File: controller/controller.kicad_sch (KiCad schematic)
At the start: 58 parts, among them J11 Conn_ARM_JTAG_SWD_10, J12 GRPB072VWQS-RC, J6 USB_C_Receptacle_USB2.0_16P, J7 USB_C_Receptacle_USB2.0_16P, J8 GRPB072VWQS-RC, J9 GRPB072VWQS-RC, U1 STM32G474RCTx, U10 PI5C3257, U11 QSBT40-7-F, U12 QSBT40-7-F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

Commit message: Controller and firwmare most pins in sync
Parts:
- added D13, D14, D15, D16, D17, D18, D19, D21: LED, symbol Device:LED
- added D20, D22: LED_ARGB, symbol Device:LED_ARGB
- added R25, R26: 0R, Resistor_SMD:R_0402_1005Metric, symbol Device:R_Small
- added RV2, RV3: R_Potentiometer, symbol Device:R_Potentiometer
- R69: footprint (none) -> Resistor_SMD:R_0402_1005Metric
- R70, R73: footprint Resistor_SMD:R_0603_1608Metric -> Resistor_SMD:R_0402_1005Metric
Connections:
- net +3V3: now also D16.2 (A), D17.2 (A), D18.2 (A), D19.2 (A), D21.2 (A), D22.1 (A), R26.2, RV2.1, RV3.1
- net +5V: now also R25.2
- net ADC2_IN10: no longer U1.6 (PF1)
- net ADC2_IN11: now also D19.1 (K)
- net Earth: now also RV2.3, RV3.3
- net FB_B: now also U1.6 (PF1)
- net FB_D: now also U1.22 (PC4)
- net HI_4: now also U8.13 (I1c); no longer U8.3 (I1a)
- net HI_5: now also U8.3 (I1a); no longer U8.13 (I1c)
- net HRTIM1_EEV3: no longer U1.60 (PB7)
- net HRTIM1_EEV5: no longer U1.62 (PB9)
- net HRTIM1_EEV6: no longer U1.58 (PB5)
- net HRTIM1_FLT3: no longer U1.30 (PB10)
- net LI_4: now also U8.10 (I1d); no longer U8.6 (I1b)
- net LI_5: now also U8.6 (I1b); no longer U8.10 (I1d)
- net PC2: now also D21.1 (K)
- net pwm_led5 pot2: now reaches U1.17 (PA3)
- net pwm_led5 pot2: now also D17.1 (K), D22.3 (GK), RV2.2
- net pwm_led6 pot3: now reaches U1.25 (PB1)
- net pwm_led6 pot3: now also D18.1 (K), D22.4 (BK), RV3.2
- new net: D13.2 (A), D14.2 (A), D15.2 (A), D20.1 (A), R25.1, R26.1
- new net pwm_led1: D13.1 (K), D20.2 (RK), U1.58 (PB5)
- new net pwm_led2: D14.1 (K), D20.3 (GK), U1.60 (PB7)
- new net pwm_led3: D15.1 (K), D20.4 (BK), U1.62 (PB9)
- new net pwm_led4: D16.1 (K), D22.2 (RK), U1.30 (PB10)
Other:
- note removed: "Update to match firmware"
- moved on the sheet: R72, U8

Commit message: Controller - some more changes
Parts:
- added C29, C30, C31, C32, C34: 10nF, Capacitor_SMD:C_0402_1005Metric, symbol Device:C_Small
- added R28, R29, R30, R32: 0R, Resistor_SMD:R_0402_1005Metric, symbol Device:R_Small
- added R33, R34, R36, R37, R38, R40, R47, R48: ?, Resistor_SMD:R_0402_1005Metric, symbol Device:R_Small
- D20: value LED_ARGB -> CLMUD-FKC-CHJNPM569ABB845343; footprint (none) -> Library:LED_Cree-PLCC4_1.5x1.5mm
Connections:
- net Current_sense_1B: now also R28.2
- net Current_sense_2B: now also R29.2
- net Current_sense_4: now also R29.1
- net Current_sense_5: now also R28.1
- net Earth: now also C29.2, C30.2, C31.2, C32.2, C34.2
- net FB_A: now also R30.2, R32.2
- net PB2: now also C34.1
- net PC2: now also C32.1, R48.1; no longer D21.1 (K)
- net pwm_led1: now also R33.1; no longer D13.1 (K), D20.2 (RK)
- net pwm_led2: now also R34.1; no longer D14.1 (K), D20.3 (GK)
- net pwm_led3: now also R36.1; no longer D15.1 (K), D20.4 (BK)
- net pwm_led4: now also R37.1; no longer D16.1 (K), D22.2 (RK)
- net pwm_led5 pot2: now also C30.1, R30.1, R38.1; no longer D17.1 (K), D22.3 (GK)
- net pwm_led6 pot3: now also C31.1, R40.1; no longer D18.1 (K), D22.4 (BK)
- net ADC2_IN11: no longer names the net of D19.1 (K)
- net ADC2_IN11: now also R47.2; no longer U1.23 (PC5)
- new net: D13.1 (K), D20.2 (RK), R33.2
- new net: D16.1 (K), D22.2 (RK), R37.2
- new net: D18.1 (K), D22.4 (BK), R40.2
- new net: D17.1 (K), D22.3 (GK), R38.2
- new net: D15.1 (K), D20.4 (BK), R36.2
- new net: D14.1 (K), D20.3 (GK), R34.2
- new net: D21.1 (K), R48.2
- new net pwm_led7: C29.1, R32.1, R47.1, U1.23 (PC5)
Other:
- note added: "Kolla så esp kan output på LED-pinnar"
- note added: "Route FB_A"
- moved on the sheet: RV2

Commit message: Controller - more changes
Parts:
- D22: footprint (none) -> Library:LED_Cree-PLCC4_1.5x1.5mm
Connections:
- net PC2: now also R37.1; no longer R48.1
- net pwm_led4: now also R38.1; no longer R37.1
- net pwm_led5 pot2: now also R48.1; no longer R38.1
- net pwm_led6 pot3: now also R47.1; no longer R40.1
- net pwm_led7: now also R40.1; no longer R47.1
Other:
- sheet esp32c6 ports: added B_BOOT, G, R; removed none
- note removed: "V_{GS} >= 100V"
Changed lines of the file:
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@@
 	(wire
 		(pts
-			(xy 171.45 170.18) (xy 186.69 170.18)
-		)
-		(stroke
-			(width 0)
-			(type default)
-		)
-	)
-	(wire
-		(pts
 			(xy 427.99 72.39) (xy 454.66 72.39)
 		)
@@
 	(wire
 		(pts
+			(xy 177.8 172.72) (xy 171.45 172.72)
+		)
+		(stroke
+			(width 0)
+			(type default)
+		)
+	)
+	(wire
+		(pts
 			(xy 167.64 97.79) (xy 179.07 97.79)
 		)
@@
 	(wire
 		(pts
-			(xy 55.88 407.67) (xy 63.5 407.67)
-		)
-		(stroke
-			(width 0)
-			(type default)
-		)
-	)
-	(wire
-		(pts
 			(xy 434.34 163.83) (xy 438.15 163.83)
 		)
@@
 	(wire
 		(pts
+			(xy 182.88 170.18) (xy 171.45 170.18)
+		)
+		(stroke
+			(width 0)
+			(type default)
+		)
+	)
+	(wire
+		(pts
 			(xy 167.64 77.47) (xy 185.42 77.47)
 		)
@@
 	(wire
 		(pts
-			(xy 171.45 167.64) (xy 193.04 167.64)
+			(xy 171.45 163.83) (xy 193.04 163.83)
 		)
 		(stroke
@@
 	(wire
 		(pts
+			(xy 171.45 166.37) (xy 186.69 166.37)
+		)
+		(stroke
+			(width 0)
+			(type default)
+		)
+	)
+	(wire
+		(pts
 			(xy 303.53 281.94) (xy 303.53 280.67)
 		)
@@
 	(wire
 		(pts
+			(xy 182.88 175.26) (xy 171.45 175.26)
+		)
+		(stroke
+			(width 0)
+			(type default)
+		)
+	)
+	(wire
+		(pts
 			(xy 88.9 278.13) (xy 76.2 278.13)
 		)
@@
 	(text "Kolla så esp kan output på LED-pinnar"
 		(exclude_from_sim no)
-		(at 136.398 168.91 0)
+		(at 141.478 188.976 0)
 		(effects
 			(font
@@
 		)
 	)
-	(text "V_{GS} >= 100V"
-		(exclude_from_sim no)
-		(at 72.644 406.4 0)
-		(effects
-			(font
-				(size 1.27 1.27)
-			)
-		)
-	)
 	(text "page 37 layout i https://www.ti.com/lit/ds/symlink/lm5168.pdf?ts=1714923464346"
 		(exclude_from_sim no)
@@
 	)
 	(label "pwm_led5 pot2"
-		(at 430.53 185.42 270)
+		(at 450.85 185.42 270)
 		(fields_autoplaced yes)
 		(effects
@@
 		)
 	)
+	(label "pwm_led4"
+		(at 182.88 175.26 180)
+		(fields_autoplaced yes)
+		(effects
+			(font
+				(size 1.27 1.27)
+			)
+			(justify right bottom)
+		)
+	)
 	(label "NTC_2"
 		(at 124.46 80.01 0)
@@
 	)
 	(label "pwm_led4"
-		(at 424.18 185.42 270)
+		(at 430.53 185.42 270)
 		(fields_autoplaced yes)
 		(effects
@@
 	)
 	(label "pwm_led7"
-		(at 444.5 185.42 270)
+		(at 438.15 185.42 270)
 		(fields_autoplaced yes)
 		(effects
@@
 	)
 	(label "PC2"
-		(at 450.85 185.42 270)
+		(at 424.18 185.42 270)
 		(fields_autoplaced yes)
 		(effects
@@
 	)
 	(label "STM32_NRST_TO_ESP"
-		(at 193.04 167.64 180)
+		(at 193.04 163.83 180)
+		(fields_autoplaced yes)
+		(effects
+			(font
+				(size 1.27 1.27)
+			)
+			(justify right bottom)
+		)
+	)
+	(label "pwm_led7"
+		(at 182.88 170.18 180)
 		(fields_autoplaced yes)
 		(effects
@@
 	)
 	(label "STM32_BOOT0"
-		(at 186.69 170.18 180)
+		(at 186.69 166.37 180)
 		(fields_autoplaced yes)
 		(effects
@@
 		)
 	)
+	(label "PC2"
+		(at 177.8 172.72 180)
+		(fields_autoplaced yes)
+		(effects
+			(font
+				(size 1.27 1.27)
+			)
+			(justify right bottom)
+		)
+	)
 	(label "STM32_SWC"
 		(at 181.61 85.09 180)
@@
 	)
 	(label "pwm_led6 pot3"
-		(at 438.15 185.42 270)
+		(at 444.5 185.42 270)
 		(fields_autoplaced yes)
 		(effects
@@
 			)
 		)
-		(property "Footprint" ""
+		(property "Footprint" "Library:LED_Cree-PLCC4_1.5x1.5mm"
 			(at 412.75 166.37 0)
 			(effects
@@
 	)
 	(symbol
-		(lib_id "power:Earth")
-		(at 55.88 407.67 0)
-		(unit 1)
-		(exclude_from_sim no)
-		(in_bom yes)
-		(on_board yes)
-		(dnp no)
-		(fields_autoplaced yes)
-		(property "Reference" "#PWR0122"
-			(at 55.88 414.02 0)
-			(effects
-				(font
-					(size 1.27 1.27)
-				)
-				(hide yes)
-			)
-		)
-		(property "Value" "Earth"
-			(at 55.88 411.48 0)
-			(effects
-				(font
-					(size 1.27 1.27)
-				)
-				(hide yes)
-			)
-		)
-		(property "Footprint" ""
-			(at 55.88 407.67 0)
-			(effects
-				(font
-					(size 1.27 1.27)
-				)
-				(hide yes)
-			)
-		)
-		(property "Datasheet" "~"
-			(at 55.88 407.67 0)
-			(effects
-				(font
-					(size 1.27 1.27)
-				)
-				(hide yes)
-			)
-		)
-		(property "Description" ""
-			(at 55.88 407.67 0)
-			(effects
-				(font
-					(size 1.27 1.27)
-				)
-				(hide yes)
-			)
-		)
-		(pin "1"
-		)
-		(instances
-			(project "controller"
-				(path "/5b092a03-7e3e-4df1-ad91-2ac0e362f857"
-					(reference "#PWR0122")
-					(unit 1)
-				)
-			)
-		)
-	)
-	(symbol
 		(lib_id "74xx:74LS257")
 		(at 251.46 172.72 0)
@@
 		(at 128.27 162.56)
 		(size 43.18 13.97)
+		(fields_autoplaced yes)
 		(stroke
 			(width 0.1524)
@@
 		)
 		(property "Sheetname" "esp32c6"
-			(at 145.034 168.656 0)
+			(at 128.27 161.8484 0)
 			(effects
 				(font
@@
 		)
 		(property "Sheetfile" "esp32c6.kicad_sch"
-			(at 136.906 173.482 0)
+			(at 128.27 177.1146 0)
 			(effects
 				(font
@@
 		)
 		(pin "GPIO21" bidirectional
-			(at 171.45 170.18 0)
+			(at 171.45 166.37 0)
 			(effects
 				(font
@@
 		)
 		(pin "GPIO20" bidirectional
-			(at 171.45 167.64 0)
+			(at 171.45 163.83 0)
 			(effects
 				(font
@@
 			)
 		)
+		(pin "B_BOOT" bidirectional
+			(at 171.45 175.26 0)
+			(effects
+				(font
+					(size 1.27 1.27)
+				)
+				(justify right)
+			)
+		)
+		(pin "G" input
+			(at 171.45 172.72 0)
+			(effects
+				(font
+					(size 1.27 1.27)
+				)
+				(justify right)
+			)
+		)
+		(pin "R" output
+			(at 171.45 170.18 0)
+			(effects
+				(font
+					(size 1.27 1.27)
+				)
+				(justify right)
+			)
+		)

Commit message: Controller - Route mcu pins
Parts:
- removed R97: 100k, Resistor_SMD:R_0402_1005Metric, symbol Device:R_Small
- added C36: 10nF, Capacitor_SMD:C_0402_1005Metric, symbol Device:C_Small
- added R67: 1k, Resistor_SMD:R_0402_1005Metric, symbol Device:R_Small
- added SW3: Boot, symbol Switch:SW_Push
- added SW4: Reset, symbol Switch:SW_Push
- added U14: QSBT40-7-F, Package_TO_SOT_SMD:SOT-363_SC-70-6, symbol Library:QSBT40-7-F
- J11: footprint (none) -> Connector_PinHeader_1.27mm:PinHeader_2x05_P1.27mm_Vertical_SMD
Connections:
- net +3V3: now also SW3.1, U14.5 (VCC)
- net CC1_MCU: now also U12.3 (DL3), U12.4 (DL2); no longer U13.6 (DL1)
- net CC2_MCU: now also U12.1 (DL4), U12.6 (DL1); no longer U13.4 (DL2)
- net Earth: now also C36.2, SW4.2, U14.2 (GND)
- net FB_A: now also U14.4 (DL2), U14.6 (DL1); no longer U12.6 (DL1)
- net FB_B: now also U14.1 (DL4), U14.3 (DL3); no longer U12.4 (DL2)
- net FB_C: now also U13.1 (DL4); no longer U12.3 (DL3)
- net FB_D: now also U13.6 (DL1); no longer U12.1 (DL4)
- net PA4: now also U13.4 (DL2); no longer U13.3 (DL3)
- net PA5: now also U13.3 (DL3); no longer U13.1 (DL4)
- net STM32_BOOT0: now also R67.2; no longer U1.61 (PB8)
- net STM32_NRST_TO_CON: no longer R96.1, U9.4 (Pin_4)
- net STM32_NRST: now reaches C19.1, R69.2, R70.2, R73.2, U1.7 (PG10)
- net STM32_NRST: now also R96.1, U9.4 (Pin_4), SW4.1
- new net: C36.1, R67.1, SW3.2, U1.61 (PB8)
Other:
- note removed: "Kolla så esp kan output på LED-pinnar"
- moved on the sheet: R69, R70, R73, R94, R95, R96, U12A, U12B, U12C, U12D, U12E, U13A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

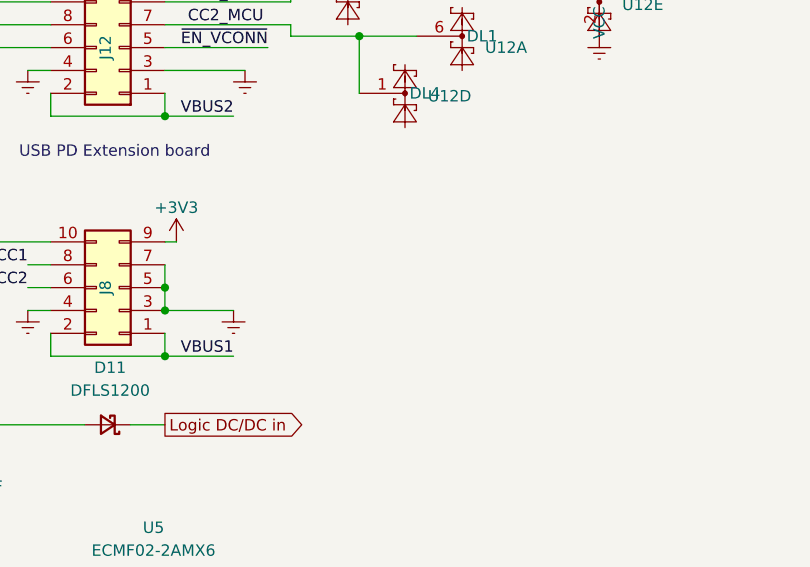
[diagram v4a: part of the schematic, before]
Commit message: Controller - Even more pins
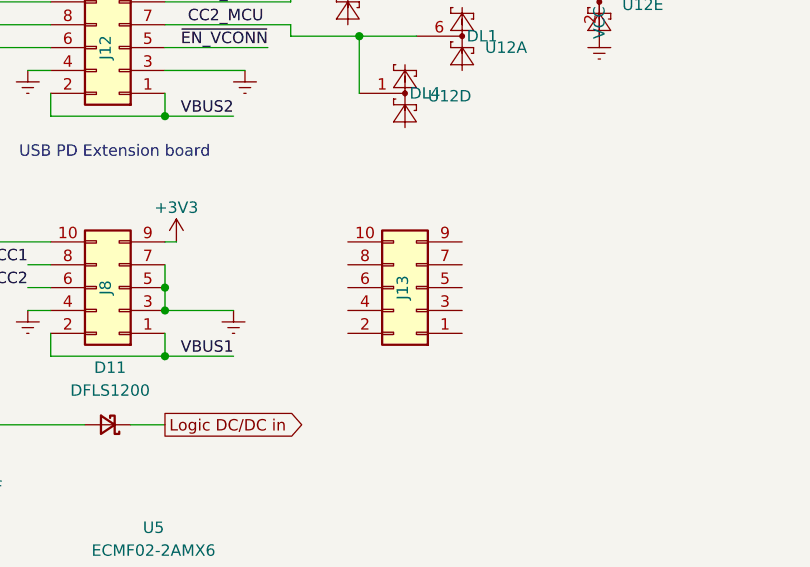
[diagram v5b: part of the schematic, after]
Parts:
- added J13: GRPB072VWQS-RC, Connector_PinHeader_1.27mm:PinHeader_2x05_P1.27mm_Vertical_SMD, symbol Connector_Generic:Conn_02x05_Odd_Even
- R74, R75: footprint Resistor_SMD:R_0805_1005Metric -> Resistor_SMD:R_0805_2012Metric
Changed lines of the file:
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@@
 			)
 		)
-		(property "Footprint" "Resistor_SMD:R_0805_1005Metric"
+		(property "Footprint" "Resistor_SMD:R_0805_2012Metric"
 			(at 332.74 30.48 0)
 			(effects
@@
 			)
 		)
-		(property "Footprint" "Resistor_SMD:R_0805_1005Metric"
+		(property "Footprint" "Resistor_SMD:R_0805_2012Metric"
 			(at 332.74 26.67 0)
 			(effects
@@
 					(unit 1)
 				)
+			)
+		)
+	)
+	(symbol
+		(lib_id "Connector_Generic:Conn_02x05_Odd_Even")
+		(at 104.14 320.04 180)
+		(unit 1)
+		(exclude_from_sim no)
+		(in_bom yes)
+		(on_board yes)
+		(dnp no)
+		(property "Reference" "J13"
+			(at 102.616 320.04 90)
+			(effects
+				(font
+					(size 1.27 1.27)
+				)
+			)
+		)
+		(property "Value" "GRPB072VWQS-RC"
+			(at 102.616 319.786 90)
+			(effects
+				(font
+					(size 1.27 1.27)
+				)
+				(hide yes)
+			)
+		)
+		(property "Footprint" "Connector_PinHeader_1.27mm:PinHeader_2x05_P1.27mm_Vertical_SMD"
+			(at 104.14 320.04 0)
+			(effects
+				(font
+					(size 1.27 1.27)
+				)
+				(hide yes)
+			)
+		)
+		(property "Datasheet" "~"
+			(at 104.14 320.04 0)
+			(effects
+				(font
+					(size 1.27 1.27)
+				)
+				(hide yes)
+			)
+		)
+		(property "Description" "Generic connector, double row, 02x05, odd/even pin numbering scheme (row 1 odd numbers, row 2 even numbers), script generated (kicad-library-utils/schlib/autogen/connector/)"
+			(at 104.14 320.04 0)
+			(effects
+				(font
+					(size 1.27 1.27)
+				)
+				(hide yes)
+			)
+		)
+		(pin "3"
+		)
+		(pin "2"
+		)
+		(pin "1"
+		)
+		(pin "6"
+		)
+		(pin "4"
+		)
+		(pin "5"
+		)
+		(pin "8"
+		)
+		(pin "9"
+		)
+		(pin "7"
+		)
+		(pin "10"
+		)
+		(instances
+			(project "controller"
+				(path "/5b092a03-7e3e-4df1-ad91-2ac0e362f857"
+					(reference "J13")
+					(unit 1)
+				)

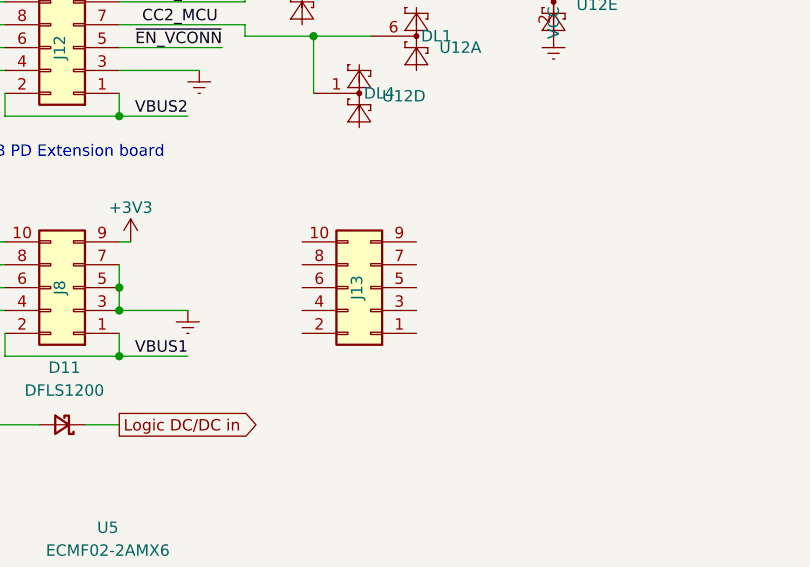
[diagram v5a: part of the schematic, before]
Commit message: Controller - Start work on vbus connection, improve rgb-led placement
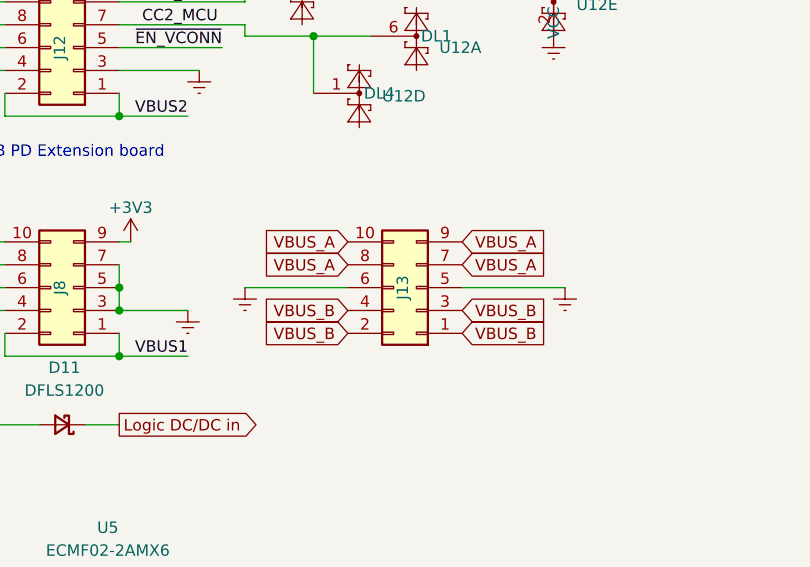
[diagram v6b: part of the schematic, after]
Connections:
- net Earth: now also J13.5 (Pin_5), J13.6 (Pin_6)
- net VBUS_B: now reaches J13.1 (Pin_1)
- net VBUS_B: now also J13.2 (Pin_2), J13.3 (Pin_3), J13.4 (Pin_4)
- net VBUS_A: now reaches J13.10 (Pin_10)
- net VBUS_A: now also J13.7 (Pin_7), J13.8 (Pin_8), J13.9 (Pin_9)
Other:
- moved on the sheet: J13

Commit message: Controller - Setup clearance, place rgb led resistors, some more routing and step down current sense
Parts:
- added R118, R119, R120, R121, R122, R123: 1k, Resistor_SMD:R_0402_1005Metric, symbol Device:R_Small
- added R124, R125, R126, R127, R128, R129: 10k, Resistor_SMD:R_0402_1005Metric, symbol Device:R_Small
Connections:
- net Current_sense_1B is gone; now on net Current_sense_1A: R28.2, U1.9 (PC1)
- net Current_sense_1A: now also U14.3 (DL3), U14.4 (DL2), R122.2, R123.2, R128.2, R129.2
- net Current_sense_2: now also R118.2, R124.2; no longer U10.4 (Za)
- net Current_sense_3: now also R119.2, R125.2; no longer U10.7 (Zb)
- net Current_sense_4: now also R120.2, R126.2; no longer U10.12 (Zc)
- net Current_sense_5: now also R121.2, R127.2; no longer U10.9 (Zd)
- net Earth: now also R124.1, R125.1, R126.1, R127.1, R128.1, R129.1
- net FB_A: no longer U14.4 (DL2)
- net FB_B: no longer U14.3 (DL3)
- new net: R119.1, U10.7 (Zb)
- new net: R121.1, U10.9 (Zd)
- new net: R118.1, U10.4 (Za)
- new net: R120.1, U10.12 (Zc)
- new net hb-card1/Current_sense_xA: R122.1
- new net hb-card1/Current_sense_xB: R123.1
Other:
- note added: "DIODES for CS1!!!! | v"
- moved on the sheet: D12, R74, R75, U13C, U14B, U14C

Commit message: Controller - Change current sensor
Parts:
- removed R119, R120, R121, R122, R123: 1k, Resistor_SMD:R_0402_1005Metric, symbol Device:R_Small
- removed R124, R125, R126, R127, R128, R129: 10k, Resistor_SMD:R_0402_1005Metric, symbol Device:R_Small
- removed U10: PI5C3257, Package_DFN_QFN:TQFN-16-1EP_3x3mm_P0.5mm_EP1.6x1.6mm, symbol 74xx:74LS257
- added C40: 10nF, Capacitor_SMD:C_0402_1005Metric, symbol Device:C_Small
- added SW5: SW_Nidec_CAS-120A1, Button_Switch_THT:SW_Slide_SPDT_Straight_CK_OS102011MS2Q, symbol Switch:SW_Nidec_CAS-120A1
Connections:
- net DIR is gone; now on an unnamed net: U1.4 (PC15)
- net +3V3: now also SW5.1 (C)
- net +5V: now also U3.3 (VI)
- net 6-18V: no longer U3.3 (VI)
- net Current_sense_1A: no longer R28.2, U1.24 (PB0), U1.9 (PC1), U14.3 (DL3), U14.4 (DL2)
- net Current_sense_2: no longer R118.2
- net Earth: now also C40.2, SW5.3 (A)
- net at R118.1: now also C40.1
- new net: R118.2, SW5.2 (B)
- new net Current_sense_1: U1.24 (PB0), U14.4 (DL2)
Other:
- sheet hb-card1 ports: added Current_sense_x; removed Current_sense_xA, Current_sense_xB
- sheet hb-card2 ports: added Current_sense_x; removed Current_sense_xA, Current_sense_xB
- sheet hb-card3 ports: added Current_sense_x; removed Current_sense_xA, Current_sense_xB
- sheet hb-card4 ports: added Current_sense_x; removed Current_sense_xA, Current_sense_xB
- sheet hb-card5 ports: added Current_sense_x; removed Current_sense_xA, Current_sense_xB
- note removed: "DIODES for CS1!!!! | v"
- moved on the sheet: R74, R75, U11A, U11B, U11C, U11D, U11E, U13B, U13C, U14B, U14C
